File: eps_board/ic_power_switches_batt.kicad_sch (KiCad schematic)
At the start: 6 parts, among them U53 MCP23008T-E/SS

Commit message: interim checkin for EPS BOM
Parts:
- C115: value 100n -> 100nF; Manufacturer (none) -> Murata; Part Number (none) -> GRM155R61E104KA87D; Tolerance (none) -> 10; Voltage (none) -> 25
- R132, R133, R134, R135: footprint Resistor_SMD:R_0603_1608Metric_Pad0.98x0.95mm_HandSolder -> Resistor_SMD:R_0402_1005Metric_Pad0.72x0.64mm_HandSolder; Manufacturer (none) -> YAGEO; Part Number (none) -> RC0402FR-071K928L; Tolerance (none) -> 1
- U53: symbol Project:MCP23008T-E_SS -> Common:MCP23008T-E_SS
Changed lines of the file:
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@@
 	)
 	(symbol
-		(lib_id "Project:MCP23008T-E_SS")
+		(lib_id "Common:MCP23008T-E_SS")
 		(at 61.595 33.02 0)
 		(unit 1)
@@
 			)
 		)
-		(property "Footprint" "Resistor_SMD:R_0603_1608Metric_Pad0.98x0.95mm_HandSolder"
+		(property "Footprint" "Resistor_SMD:R_0402_1005Metric_Pad0.72x0.64mm_HandSolder"
 			(at 173.99 40.005 0)
 			(effects
@@
 			)
 		)
-		(property "Datasheet" "~"
+		(property "Datasheet" "https://www.yageo.com/upload/media/product/products/datasheet/rchip/PYu-RC_Group_51_RoHS_L_12.pdf"
 			(at 173.99 40.005 0)
 			(effects
@@
 		)
 		(property "Description" "Resistor, small symbol"
+			(at 173.99 40.005 0)
+			(effects
+				(font
+					(size 1.27 1.27)
+				)
+				(hide yes)
+			)
+		)
+		(property "Manufacturer" "YAGEO"
+			(at 173.99 40.005 0)
+			(effects
+				(font
+					(size 1.27 1.27)
+				)
+				(hide yes)
+			)
+		)
+		(property "Part Number" "RC0402FR-071K928L"
+			(at 173.99 40.005 0)
+			(effects
+				(font
+					(size 1.27 1.27)
+				)
+				(hide yes)
+			)
+		)
+		(property "Tolerance" "1"
 			(at 173.99 40.005 0)
 			(effects
@@
 			)
 		)
-		(property "Value" "100n"
+		(property "Value" "100nF"
 			(at 125.73 43.8149 0)
 			(effects
@@
 			)
 		)
-		(property "Datasheet" "~"
+		(property "Datasheet" "https://search.murata.co.jp/Ceramy/image/img/A01X/G101/ENG/GRM155R61E104KA87-01.pdf"
 			(at 121.92 42.545 0)
 			(effects
@@
 		)
 		(property "Description" "Unpolarized capacitor"
+			(at 121.92 42.545 0)
+			(effects
+				(font
+					(size 1.27 1.27)
+				)
+				(hide yes)
+			)
+		)
+		(property "Manufacturer" "Murata"
+			(at 121.92 42.545 0)
+			(effects
+				(font
+					(size 1.27 1.27)
+				)
+				(hide yes)
+			)
+		)
+		(property "Part Number" "GRM155R61E104KA87D"
+			(at 121.92 42.545 0)
+			(effects
+				(font
+					(size 1.27 1.27)
+				)
+				(hide yes)
+			)
+		)
+		(property "Voltage" "25"
+			(at 121.92 42.545 0)
+			(effects
+				(font
+					(size 1.27 1.27)
+				)
+				(hide yes)
+			)
+		)
+		(property "Tolerance" "10"
 			(at 121.92 42.545 0)
 			(effects
@@
 			)
 		)
-		(property "Footprint" "Resistor_SMD:R_0603_1608Metric_Pad0.98x0.95mm_HandSolder"
+		(property "Footprint" "Resistor_SMD:R_0402_1005Metric_Pad0.72x0.64mm_HandSolder"
 			(at 173.99 107.95 0)
 			(effects
@@
 			)
 		)
-		(property "Datasheet" "~"
+		(property "Datasheet" "https://www.yageo.com/upload/media/product/products/datasheet/rchip/PYu-RC_Group_51_RoHS_L_12.pdf"
 			(at 173.99 107.95 0)
 			(effects
@@
 		)
 		(property "Description" "Resistor, small symbol"
+			(at 173.99 107.95 0)
+			(effects
+				(font
+					(size 1.27 1.27)
+				)
+				(hide yes)
+			)
+		)
+		(property "Manufacturer" "YAGEO"
+			(at 173.99 107.95 0)
+			(effects
+				(font
+					(size 1.27 1.27)
+				)
+				(hide yes)
+			)
+		)
+		(property "Part Number" "RC0402FR-071K928L"
+			(at 173.99 107.95 0)
+			(effects
+				(font
+					(size 1.27 1.27)
+				)
+				(hide yes)
+			)
+		)
+		(property "Tolerance" "1"
 			(at 173.99 107.95 0)
 			(effects
@@
 			)
 		)
-		(property "Footprint" "Resistor_SMD:R_0603_1608Metric_Pad0.98x0.95mm_HandSolder"
+		(property "Footprint" "Resistor_SMD:R_0402_1005Metric_Pad0.72x0.64mm_HandSolder"
 			(at 173.99 142.24 0)
 			(effects
@@
 			)
 		)
-		(property "Datasheet" "~"
+		(property "Datasheet" "https://www.yageo.com/upload/media/product/products/datasheet/rchip/PYu-RC_Group_51_RoHS_L_12.pdf"
 			(at 173.99 142.24 0)
 			(effects
@@
 		)
 		(property "Description" "Resistor, small symbol"
+			(at 173.99 142.24 0)
+			(effects
+				(font
+					(size 1.27 1.27)
+				)
+				(hide yes)
+			)
+		)
+		(property "Manufacturer" "YAGEO"
+			(at 173.99 142.24 0)
+			(effects
+				(font
+					(size 1.27 1.27)
+				)
+				(hide yes)
+			)
+		)
+		(property "Part Number" "RC0402FR-071K928L"
+			(at 173.99 142.24 0)
+			(effects
+				(font
+					(size 1.27 1.27)
+				)
+				(hide yes)
+			)
+		)
+		(property "Tolerance" "1"
 			(at 173.99 142.24 0)
 			(effects
@@
 			)
 		)
-		(property "Footprint" "Resistor_SMD:R_0603_1608Metric_Pad0.98x0.95mm_HandSolder"
+		(property "Footprint" "Resistor_SMD:R_0402_1005Metric_Pad0.72x0.64mm_HandSolder"
 			(at 173.99 74.295 0)
 			(effects
@@
 			)
 		)
-		(property "Datasheet" "~"
+		(property "Datasheet" "https://www.yageo.com/upload/media/product/products/datasheet/rchip/PYu-RC_Group_51_RoHS_L_12.pdf"
 			(at 173.99 74.295 0)
 			(effects
@@
 			(at 173.99 74.295 0)
 			(effects
+				(font
+					(size 1.27 1.27)
+				)
+				(hide yes)
+			)
+		)
+		(property "Manufacturer" "YAGEO"
+			(at 173.99 74.295 0)
+			(effects
+				(font
+					(size 1.27 1.27)
+				)
+				(hide yes)
+			)
+		)
+		(property "Part Number" "RC0402FR-071K928L"
+			(at 173.99 74.295 0)
+			(effects
+				(font
+					(size 1.27 1.27)
+				)
+				(hide yes)
+			)
+		)
+		(property "Tolerance" "1"
+			(at 173.99 74.295 0)
+			(effects

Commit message: complete BOM assignment for EPS, next step circular check and deep dives
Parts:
- U53: Manufacturer (none) -> Microchip; Part Number (none) -> MCP23008T-E/SS
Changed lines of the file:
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@@
 			)
 		)
-		(property "Datasheet" "MCP23008T-E/SS"
+		(property "Datasheet" "https://ww1.microchip.com/downloads/en/DeviceDoc/MCP23008-MCP23S08-Data-Sheet-20001919F.pdf"
 			(at 69.215 33.02 0)
 			(effects
@@
 			(effects
 				(font
+					(size 1.27 1.27)
+				)
+				(hide yes)
+			)
+		)
+		(property "Manufacturer" "Microchip"
+			(at 61.595 33.02 0)
+			(effects
+				(font
+					(size 1.27 1.27)
+				)
+				(hide yes)
+			)
+		)
+		(property "Part Number" "MCP23008T-E/SS"
+			(at 61.595 33.02 0)
+			(effects
+				(font

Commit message: add decorations and labels to PCBs part 2
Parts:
- R132, R133, R134, R135: footprint Resistor_SMD:R_0402_1005Metric_Pad0.72x0.64mm_HandSolder -> Resistor_SMD:R_0603_1608Metric_Pad0.98x0.95mm_HandSolder; Part Number RC0402FR-071K928L -> RC0603FR-071K928L
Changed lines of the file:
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@@
 			)
 		)
-		(property "Footprint" "Resistor_SMD:R_0402_1005Metric_Pad0.72x0.64mm_HandSolder"
+		(property "Footprint" "Resistor_SMD:R_0603_1608Metric_Pad0.98x0.95mm_HandSolder"
 			(at 173.99 40.005 0)
 			(effects
@@
 			)
 		)
-		(property "Part Number" "RC0402FR-071K928L"
+		(property "Part Number" "RC0603FR-071K928L"
 			(at 173.99 40.005 0)
 			(effects
@@
 			)
 		)
-		(property "Footprint" "Resistor_SMD:R_0402_1005Metric_Pad0.72x0.64mm_HandSolder"
+		(property "Footprint" "Resistor_SMD:R_0603_1608Metric_Pad0.98x0.95mm_HandSolder"
 			(at 173.99 107.95 0)
 			(effects
@@
 			)
 		)
-		(property "Part Number" "RC0402FR-071K928L"
+		(property "Part Number" "RC0603FR-071K928L"
 			(at 173.99 107.95 0)
 			(effects
@@
 			)
 		)
-		(property "Footprint" "Resistor_SMD:R_0402_1005Metric_Pad0.72x0.64mm_HandSolder"
+		(property "Footprint" "Resistor_SMD:R_0603_1608Metric_Pad0.98x0.95mm_HandSolder"
 			(at 173.99 142.24 0)
 			(effects
@@
 			)
 		)
-		(property "Part Number" "RC0402FR-071K928L"
+		(property "Part Number" "RC0603FR-071K928L"
 			(at 173.99 142.24 0)
 			(effects
@@
 			)
 		)
-		(property "Footprint" "Resistor_SMD:R_0402_1005Metric_Pad0.72x0.64mm_HandSolder"
+		(property "Footprint" "Resistor_SMD:R_0603_1608Metric_Pad0.98x0.95mm_HandSolder"
 			(at 173.99 74.295 0)
 			(effects
@@
 			)
 		)
-		(property "Part Number" "RC0402FR-071K928L"
+		(property "Part Number" "RC0603FR-071K928L"
 			(at 173.99 74.295 0)
 			(effects

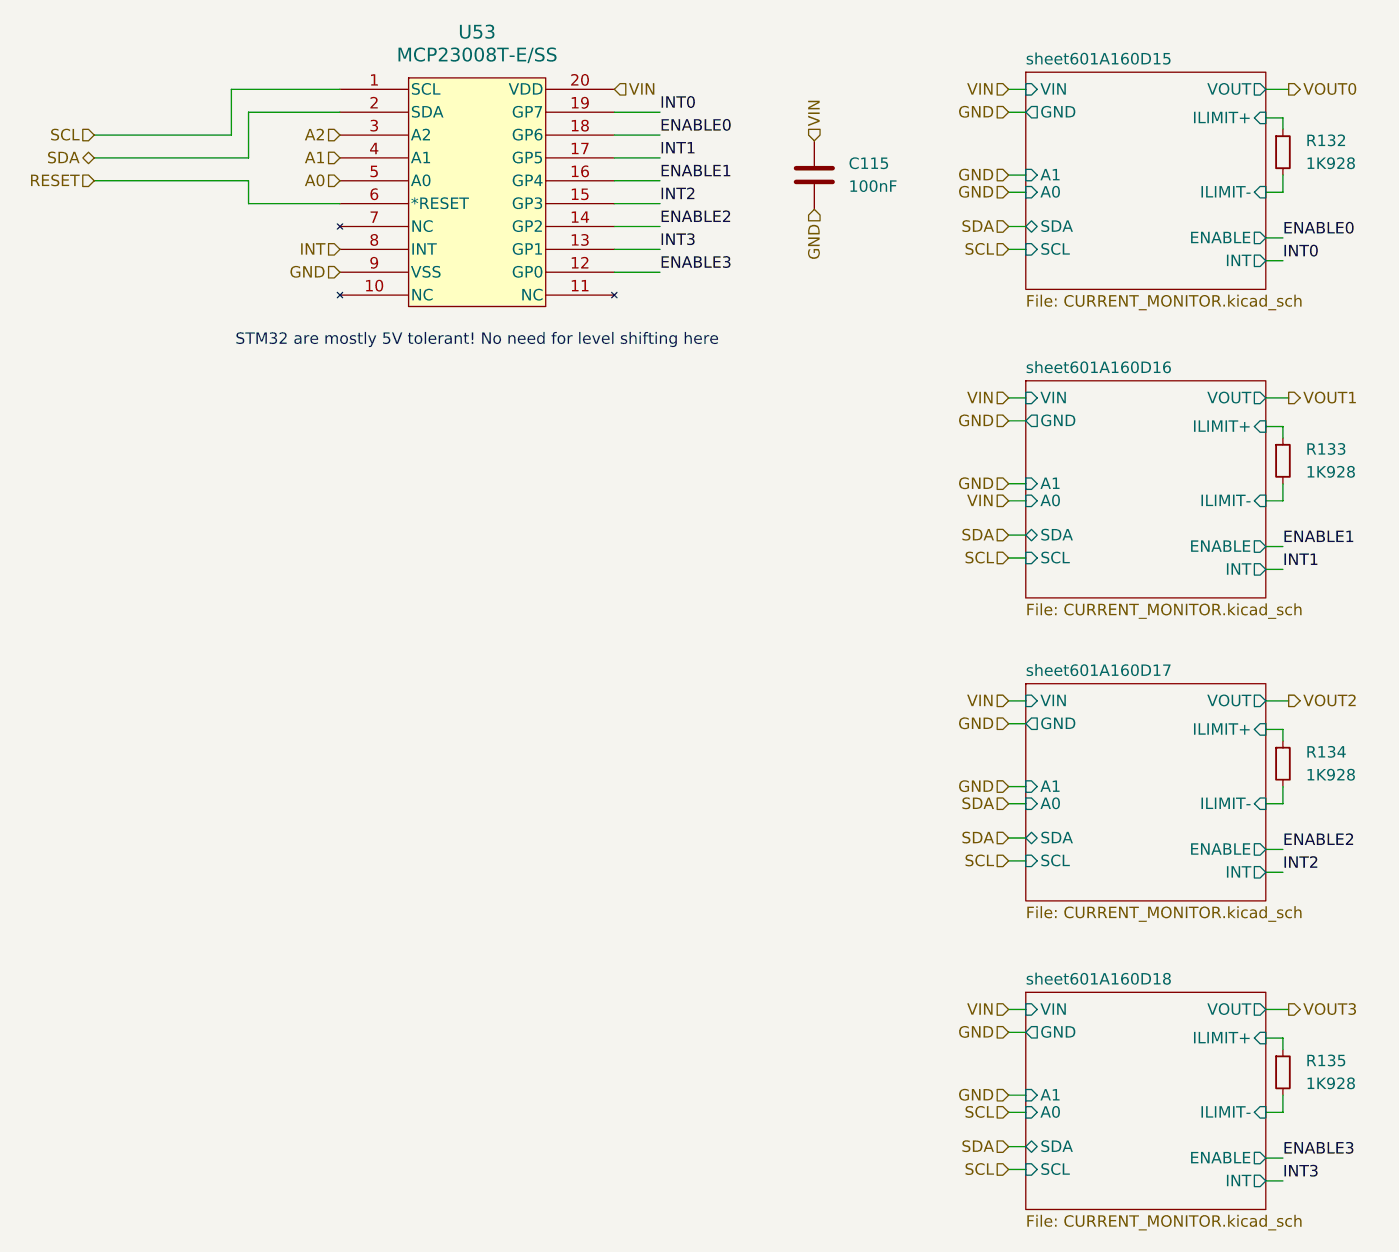
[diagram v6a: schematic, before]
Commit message: use small connectors in corners and on sides for sun sensors and solar cells
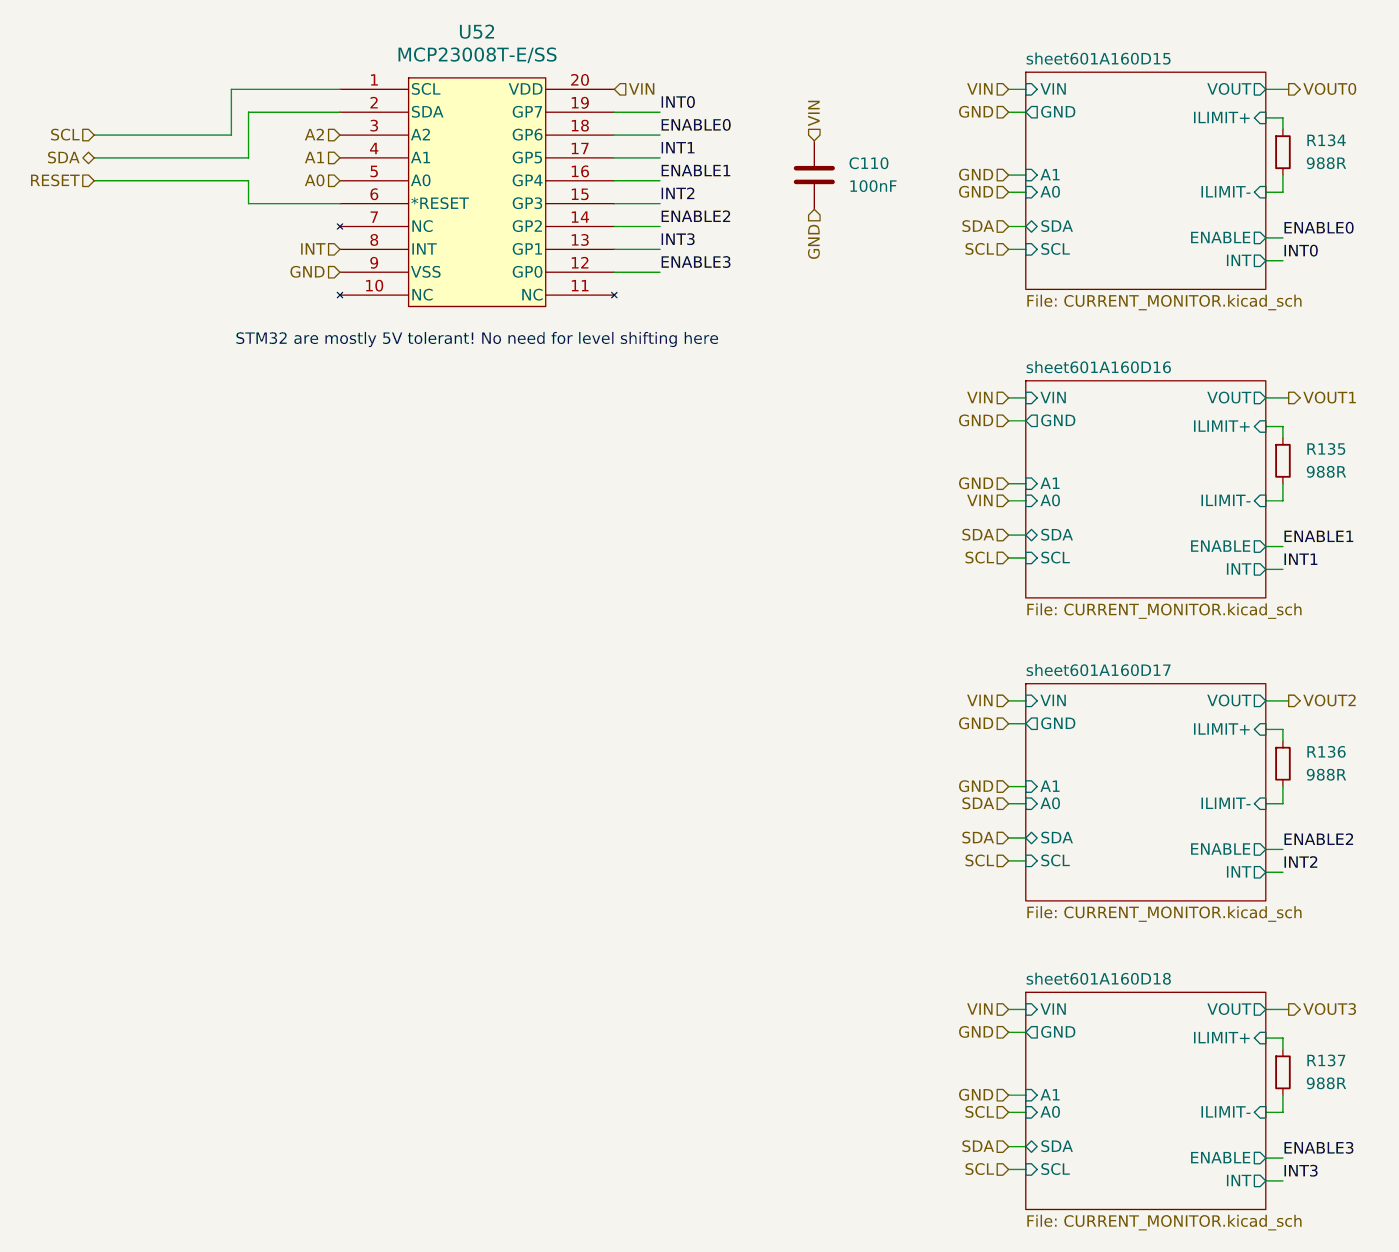
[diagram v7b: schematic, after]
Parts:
- R134: renamed from R132; value 1K928 -> 988R; Part Number RC0603FR-071K928L -> RT0603DRE07988RL; Tolerance 1 -> 0.5
- R135: renamed from R133; value 1K928 -> 988R; Part Number RC0603FR-071K928L -> RT0603DRE07988RL; Tolerance 1 -> 0.5
- R136: renamed from R134; value 1K928 -> 988R; Part Number RC0603FR-071K928L -> RT0603DRE07988RL; Tolerance 1 -> 0.5
- R137: renamed from R135; value 1K928 -> 988R; Part Number RC0603FR-071K928L -> RT0603DRE07988RL; Tolerance 1 -> 0.5
- renumbered C115 to C110, U53 to U52
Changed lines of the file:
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@@
 		(dnp no)
 		(fields_autoplaced yes)
-		(property "Reference" "U53"
+		(property "Reference" "U52"
 			(at 84.455 26.67 0)
 			(effects
@@
 		)
 		(property "Part Number" "MCP23008T-E/SS"
+			(at 61.595 33.02 0)
+			(effects
+				(font
+					(size 1.27 1.27)
+				)
+				(hide yes)
+			)
+		)
+		(property "Manufactorer" ""
 			(at 61.595 33.02 0)
 			(effects
@@
 			(project "EPS"
 				(path "/05170af6-30ef-4c3a-b972-f098085da1bc/11ac4e4f-a41f-43ab-96d4-6191a21d3d63"
-					(reference "U53")
+					(reference "U52")
 					(unit 1)
 				)
@@
 		(dnp no)
 		(fields_autoplaced yes)
-		(property "Reference" "R132"
+		(property "Reference" "R134"
 			(at 176.53 38.7349 0)
 			(effects
@@
 			)
 		)
-		(property "Value" "1K928"
+		(property "Value" "988R"
 			(at 176.53 41.2749 0)
 			(effects
@@
 			)
 		)
-		(property "Datasheet" "https://www.yageo.com/upload/media/product/products/datasheet/rchip/PYu-RC_Group_51_RoHS_L_12.pdf"
+		(property "Datasheet" "https://www.yageo.com/upload/media/product/app/datasheet/rchip/pyu-rt_1-to-0.01_rohs_l.pdf"
 			(at 173.99 40.005 0)
 			(effects
@@
 			)
 		)
-		(property "Part Number" "RC0603FR-071K928L"
+		(property "Part Number" "RT0603DRE07988RL"
 			(at 173.99 40.005 0)
 			(effects
@@
 			)
 		)
-		(property "Tolerance" "1"
+		(property "Tolerance" "0.5"
+			(at 173.99 40.005 0)
+			(effects
+				(font
+					(size 1.27 1.27)
+				)
+				(hide yes)
+			)
+		)
+		(property "Manufactorer" ""
 			(at 173.99 40.005 0)
 			(effects
@@
 			(project "EPS"
 				(path "/05170af6-30ef-4c3a-b972-f098085da1bc/11ac4e4f-a41f-43ab-96d4-6191a21d3d63"
-					(reference "R132")
+					(reference "R134")
 					(unit 1)
 				)
@@
 		(dnp no)
 		(fields_autoplaced yes)
-		(property "Reference" "C115"
+		(property "Reference" "C110"
 			(at 125.73 41.2749 0)
 			(effects
@@
 		)
 		(property "Tolerance" "10"
+			(at 121.92 42.545 0)
+			(effects
+				(font
+					(size 1.27 1.27)
+				)
+				(hide yes)
+			)
+		)
+		(property "Manufactorer" ""
 			(at 121.92 42.545 0)
 			(effects
@@
 			(project "EPS"
 				(path "/05170af6-30ef-4c3a-b972-f098085da1bc/11ac4e4f-a41f-43ab-96d4-6191a21d3d63"
-					(reference "C115")
+					(reference "C110")
 					(unit 1)
 				)
@@
 		(dnp no)
 		(fields_autoplaced yes)
-		(property "Reference" "R134"
+		(property "Reference" "R136"
 			(at 176.53 106.6799 0)
 			(effects
@@
 			)
 		)
-		(property "Value" "1K928"
+		(property "Value" "988R"
 			(at 176.53 109.2199 0)
 			(effects
@@
 			)
 		)
-		(property "Datasheet" "https://www.yageo.com/upload/media/product/products/datasheet/rchip/PYu-RC_Group_51_RoHS_L_12.pdf"
+		(property "Datasheet" "https://www.yageo.com/upload/media/product/app/datasheet/rchip/pyu-rt_1-to-0.01_rohs_l.pdf"
 			(at 173.99 107.95 0)
 			(effects
@@
 			)
 		)
-		(property "Part Number" "RC0603FR-071K928L"
+		(property "Part Number" "RT0603DRE07988RL"
 			(at 173.99 107.95 0)
 			(effects
@@
 			)
 		)
-		(property "Tolerance" "1"
+		(property "Tolerance" "0.5"
+			(at 173.99 107.95 0)
+			(effects
+				(font
+					(size 1.27 1.27)
+				)
+				(hide yes)
+			)
+		)
+		(property "Manufactorer" ""
 			(at 173.99 107.95 0)
 			(effects
@@
 			(project "EPS"
 				(path "/05170af6-30ef-4c3a-b972-f098085da1bc/11ac4e4f-a41f-43ab-96d4-6191a21d3d63"
-					(reference "R134")
+					(reference "R136")
 					(unit 1)
 				)
@@
 		(dnp no)
 		(fields_autoplaced yes)
-		(property "Reference" "R135"
+		(property "Reference" "R137"
 			(at 176.53 140.9699 0)
 			(effects
@@
 			)
 		)
-		(property "Value" "1K928"
+		(property "Value" "988R"
 			(at 176.53 143.5099 0)
 			(effects
@@
 			)
 		)
-		(property "Datasheet" "https://www.yageo.com/upload/media/product/products/datasheet/rchip/PYu-RC_Group_51_RoHS_L_12.pdf"
+		(property "Datasheet" "https://www.yageo.com/upload/media/product/app/datasheet/rchip/pyu-rt_1-to-0.01_rohs_l.pdf"
 			(at 173.99 142.24 0)
 			(effects
@@
 			)
 		)
-		(property "Part Number" "RC0603FR-071K928L"
+		(property "Part Number" "RT0603DRE07988RL"
 			(at 173.99 142.24 0)
 			(effects
@@
 			)
 		)
-		(property "Tolerance" "1"
+		(property "Tolerance" "0.5"
+			(at 173.99 142.24 0)
+			(effects
+				(font
+					(size 1.27 1.27)
+				)
+				(hide yes)
+			)
+		)
+		(property "Manufactorer" ""
 			(at 173.99 142.24 0)
 			(effects
@@
 			(project "EPS"
 				(path "/05170af6-30ef-4c3a-b972-f098085da1bc/11ac4e4f-a41f-43ab-96d4-6191a21d3d63"
-					(reference "R135")
+					(reference "R137")
 					(unit 1)
 				)
@@
 		(dnp no)
 		(fields_autoplaced yes)
-		(property "Reference" "R133"
+		(property "Reference" "R135"
 			(at 176.53 73.0249 0)
 			(effects
@@
 			)
 		)
-		(property "Value" "1K928"
+		(property "Value" "988R"
 			(at 176.53 75.5649 0)
 			(effects
@@
 			)
 		)
-		(property "Datasheet" "https://www.yageo.com/upload/media/product/products/datasheet/rchip/PYu-RC_Group_51_RoHS_L_12.pdf"
+		(property "Datasheet" "https://www.yageo.com/upload/media/product/app/datasheet/rchip/pyu-rt_1-to-0.01_rohs_l.pdf"
 			(at 173.99 74.295 0)
 			(effects
@@
 			)
 		)
-		(property "Part Number" "RC0603FR-071K928L"
+		(property "Part Number" "RT0603DRE07988RL"
 			(at 173.99 74.295 0)
 			(effects
@@
 			)
 		)
-		(property "Tolerance" "1"
+		(property "Tolerance" "0.5"
+			(at 173.99 74.295 0)
+			(effects
+				(font
+					(size 1.27 1.27)
+				)
+				(hide yes)
+			)
+		)
+		(property "Manufactorer" ""
 			(at 173.99 74.295 0)
 			(effects
@@
 			(project "EPS"
 				(path "/05170af6-30ef-4c3a-b972-f098085da1bc/11ac4e4f-a41f-43ab-96d4-6191a21d3d63"
-					(reference "R133")
+					(reference "R135")
 					(unit 1)
 				)
